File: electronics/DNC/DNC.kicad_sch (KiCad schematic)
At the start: 0 parts

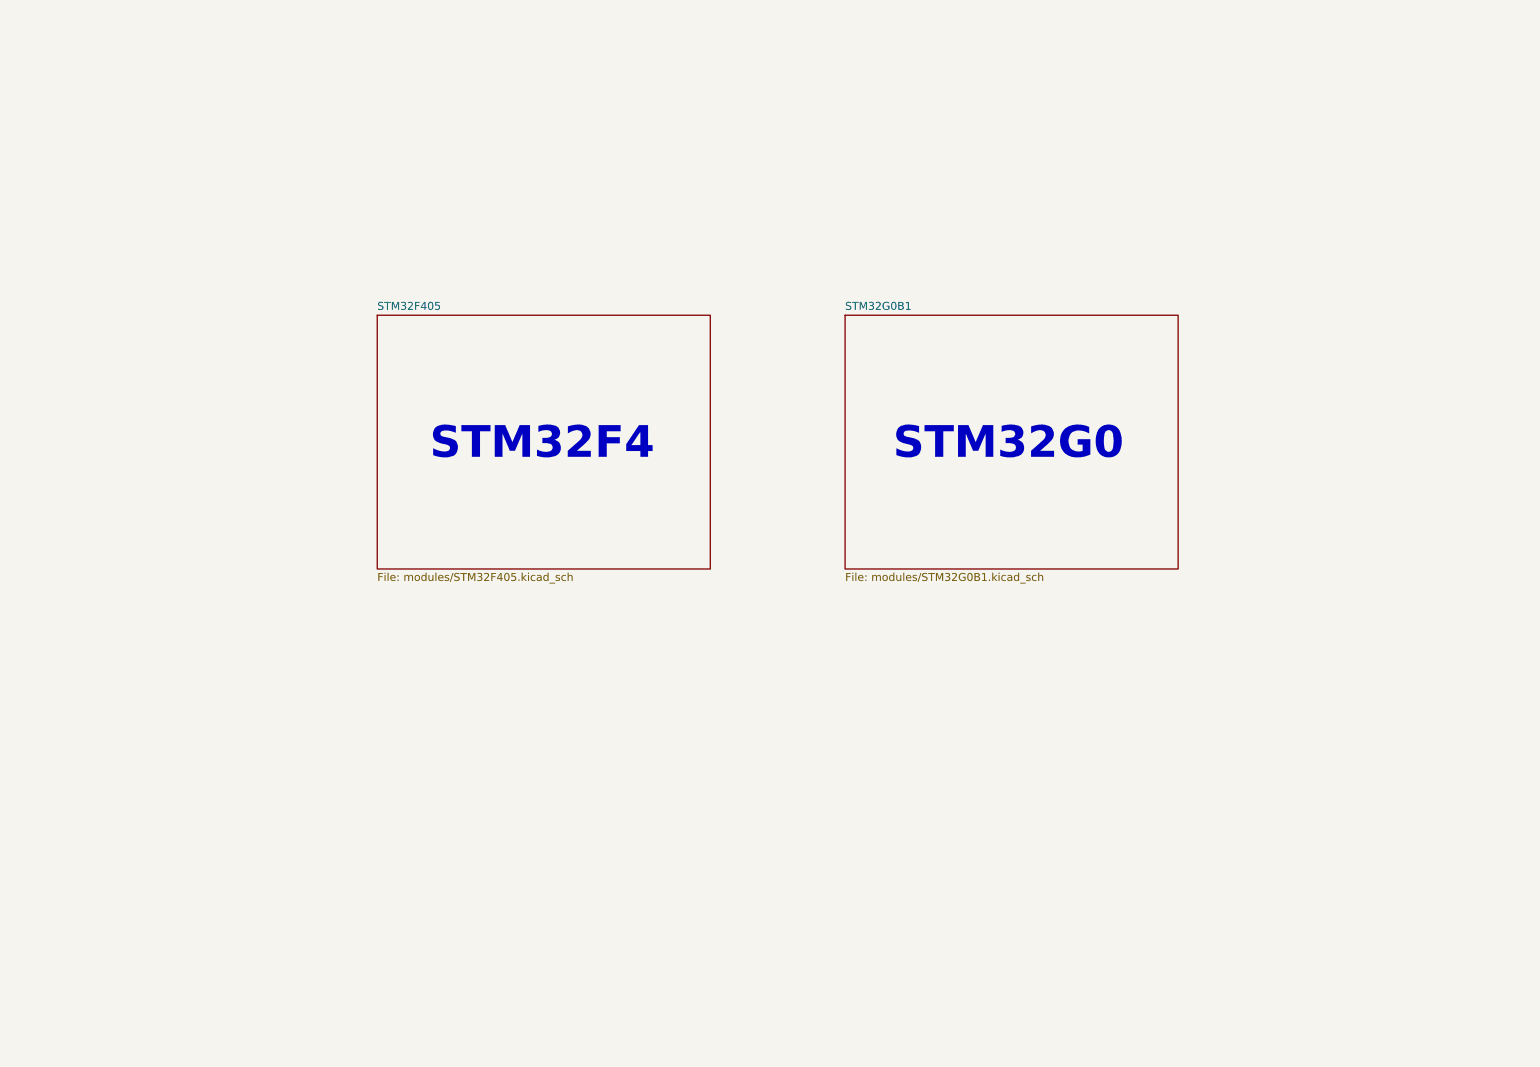
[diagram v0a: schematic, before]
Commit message: Se terminó con el diseño del STM32F4, el PMS, el ESC, el USB-TypeC y el IMU, queda pendiente que la hoja del IMU se cambie por una de sensores.
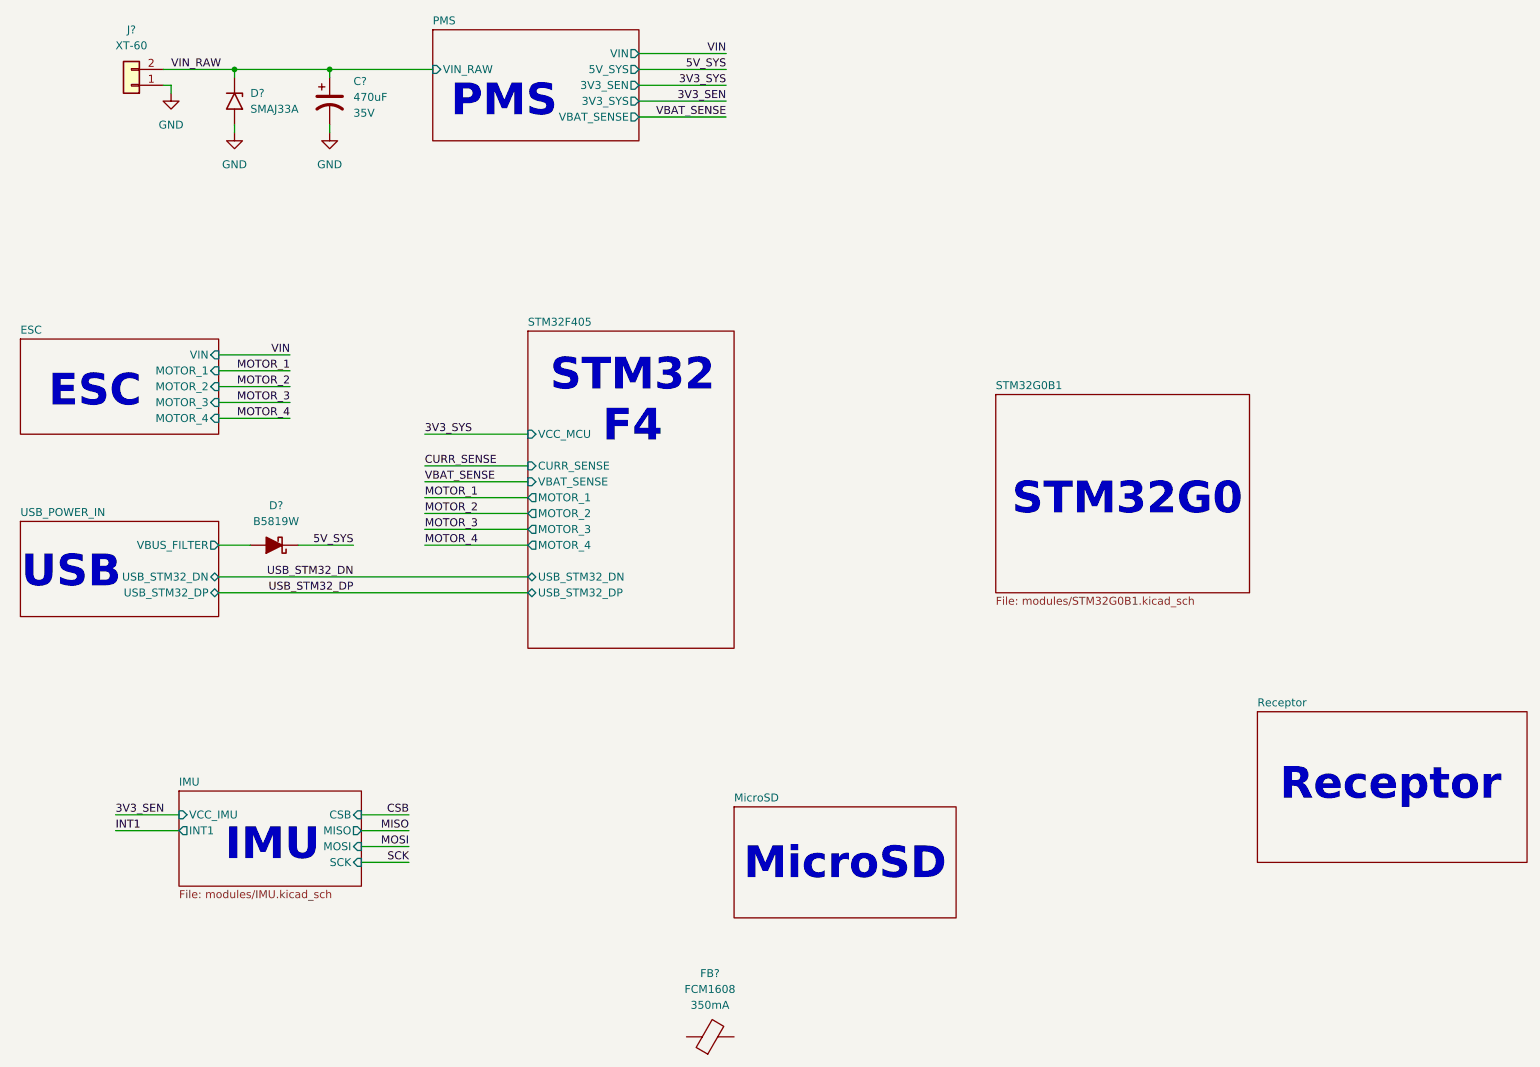
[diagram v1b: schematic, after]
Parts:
- added C?: 470uF, symbol Device:C_Polarized_US
- added D?: B5819W, symbol Device:D_Schottky_Filled
- added D?: SMAJ33A, Diode_SMD:D_SMA, symbol Diode:SMAJ33A
- added FB?: FCM1608, Inductor_SMD:L_0603_1608Metric, symbol Device:FerriteBead
- added J?: XT-60, Gen_devices:AMASS_XT60-M, symbol Connector_Generic:Conn_01x02
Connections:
- new net 5V_SYS: D?.1 (K)
- new net GND: C?.2, D?.2 (A2), J?.1 (Pin_1)
- new net USB_POWER_IN/VBUS_FILTER: D?.2 (A)
- new net VIN_RAW: C?.1, D?.1 (A1), J?.2 (Pin_2)
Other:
- added sheet ESC (modules\ESC.kicad_sch)
- added sheet IMU (modules/IMU.kicad_sch)
- added sheet MicroSD (modules\MicroSD.kicad_sch)
- added sheet PMS (modules\POWER_MANAGEMENT_SYSTEM.kicad_sch)
- added sheet Receptor (modules\Receptor.kicad_sch)
- added sheet USB_POWER_IN (modules\USB_POWER_IN.kicad_sch)
- sheet STM32F405: file modules/STM32F405.kicad_sch -> modules\STM32F405.kicad_sch
- sheet STM32F405 ports: added CURR_SENSE, MOTOR_1, MOTOR_2, MOTOR_3, MOTOR_4, USB_STM32_DN, USB_STM32_DP, VBAT_SENSE, VCC_MCU; removed none
- note added: "ESC"
- note added: "IMU"
- note added: "MicroSD"
- note added: "PMS"
- note added: "Receptor"
- note added: "STM32 F4"
- note added: "USB"
- note removed: "STM32F4"
- company: (none) -> ${COMPANY}
